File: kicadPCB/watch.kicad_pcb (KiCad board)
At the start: 2 copper layers, 81 x 53 mm, 64 parts, among them IC1 ISL1209, J1 USB_OTG, M1 BOS_LIBS_SWD_BREAKOUTS, Q1 Q_PNP_CEB, T1 BC850, U2 MKL27Z256VLH4, Y1 Crystal

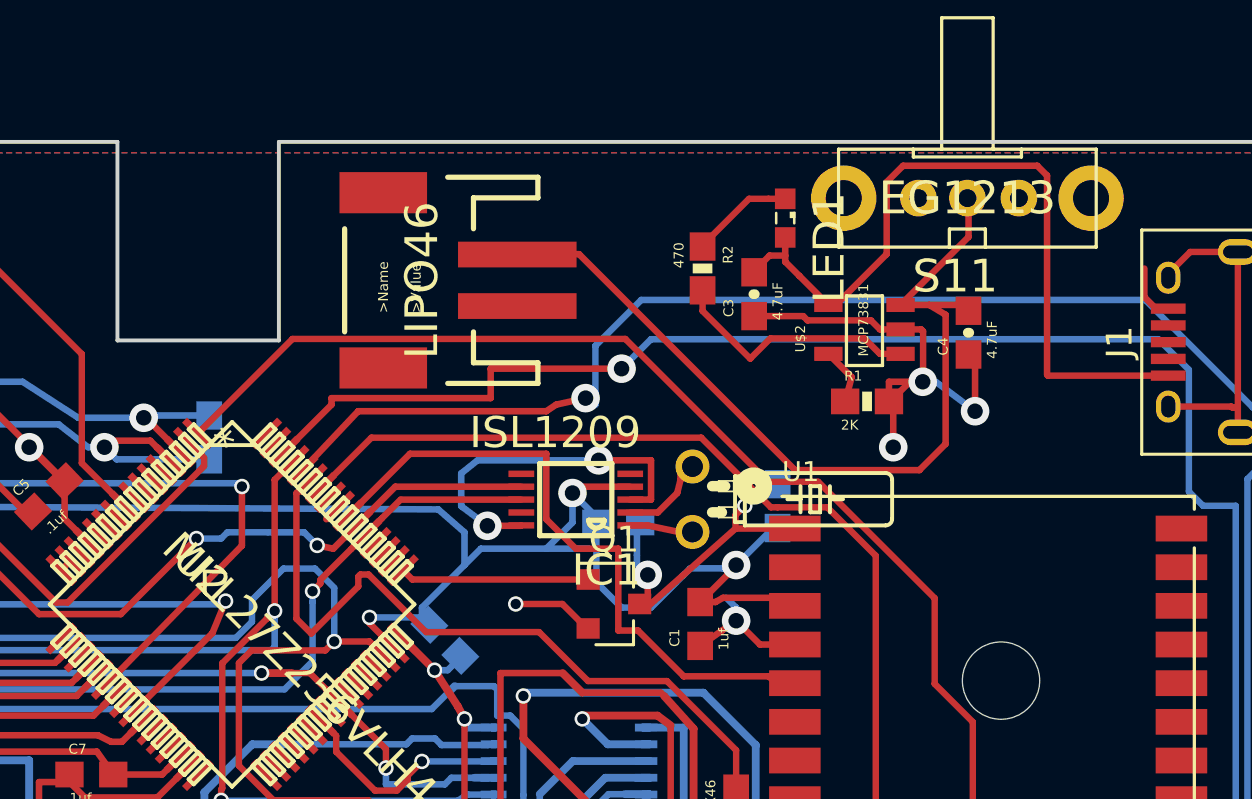
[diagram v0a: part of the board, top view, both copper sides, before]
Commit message: added pnp resistor
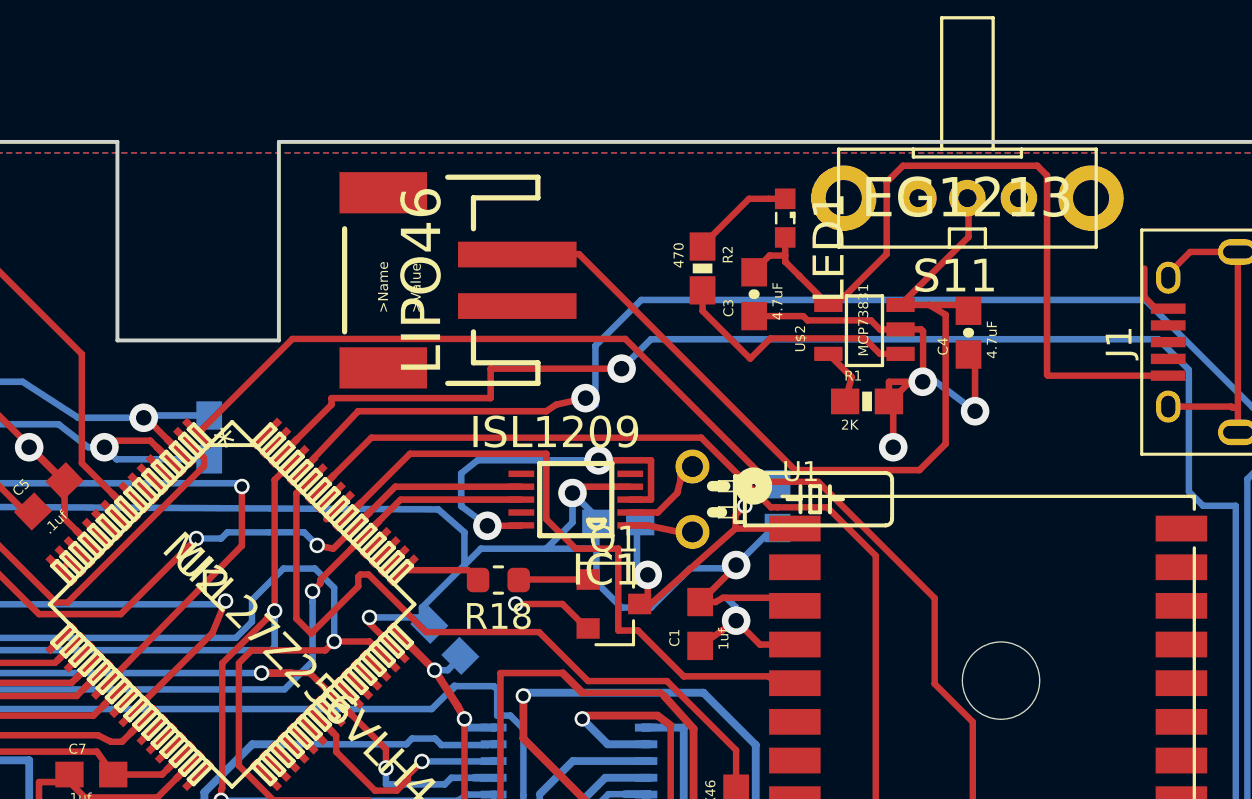
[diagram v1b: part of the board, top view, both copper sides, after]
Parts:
- added R18: 330k, Resistor_SMD:R_0603_1608Metric, F.Cu at (158.1, 95.6)
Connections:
- Q1 pad 1: /PTC4 -> Net-(Q1-Pad1)
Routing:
- net /PTC4: track 7.34 -> 3.07 mm
- net Net-(Q1-Pad1): track 0.00 -> 2.70 mm
